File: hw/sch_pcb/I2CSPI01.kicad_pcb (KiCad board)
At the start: 2 copper layers, 30 x 40.1 mm, 22 parts, among them J1 JUMP_3X2, J2 JUMP_5X2, J3 JUMP_7X2, J4 JUMP_3X2, J5 CONN_2, J6 CONN_2, J7 CONN_2, P1 _, P2 _, P3 _, P4 _, U1 SC18IS602B

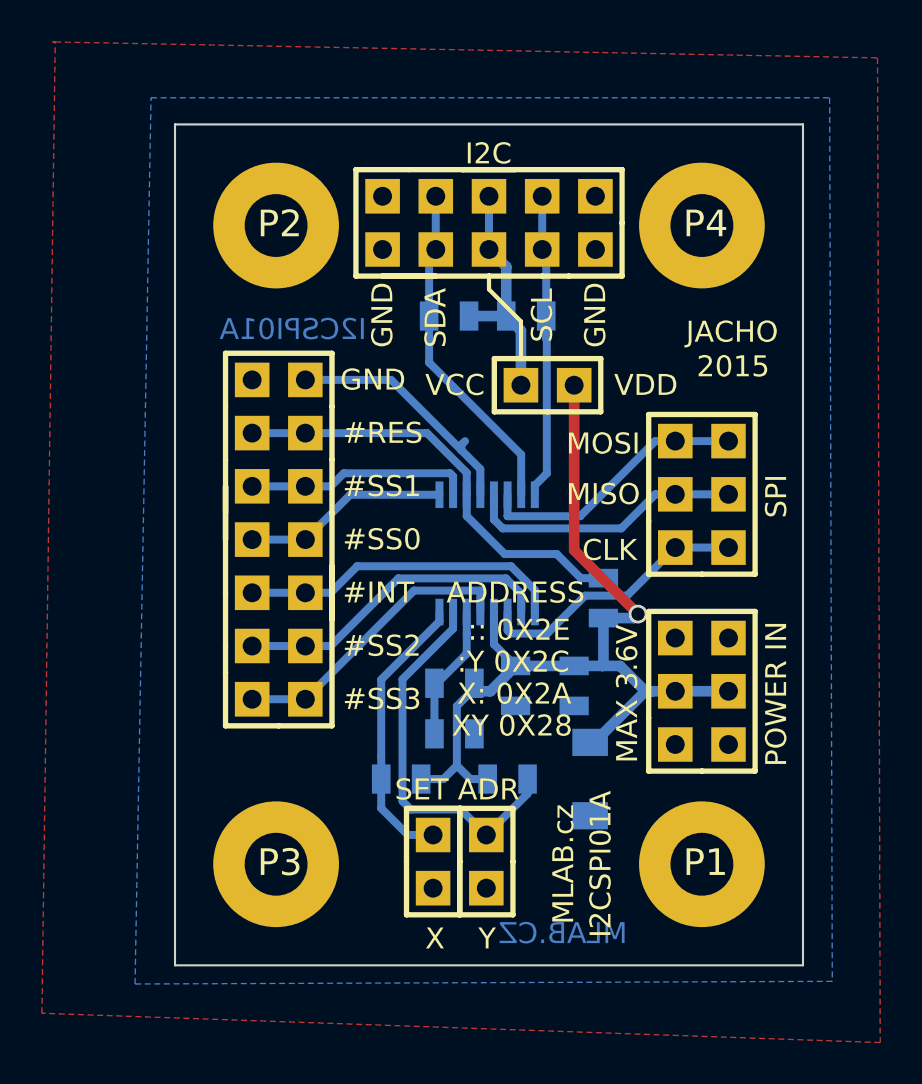
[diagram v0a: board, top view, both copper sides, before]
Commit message: Update KiCAD workflow and project data.
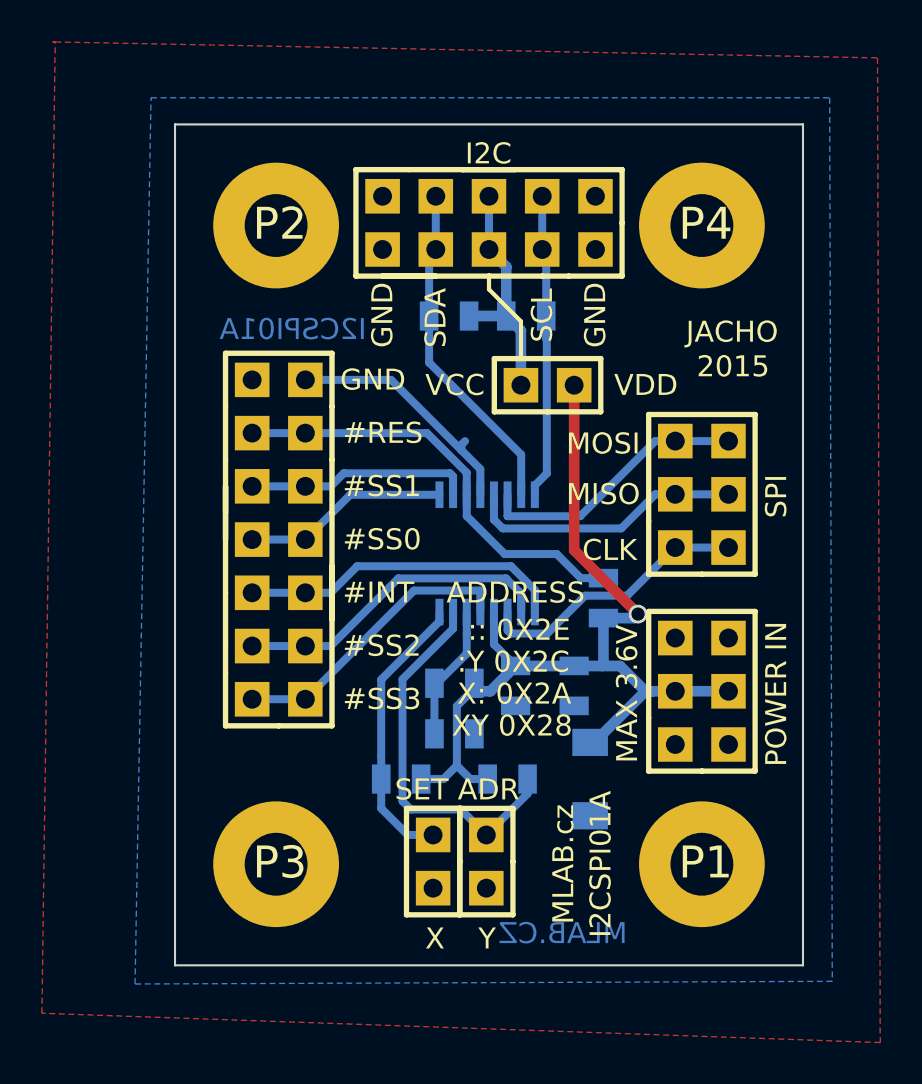
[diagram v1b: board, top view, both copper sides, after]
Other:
- net class Default removed
- net class vdd removed
